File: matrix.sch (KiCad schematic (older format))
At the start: 166 parts

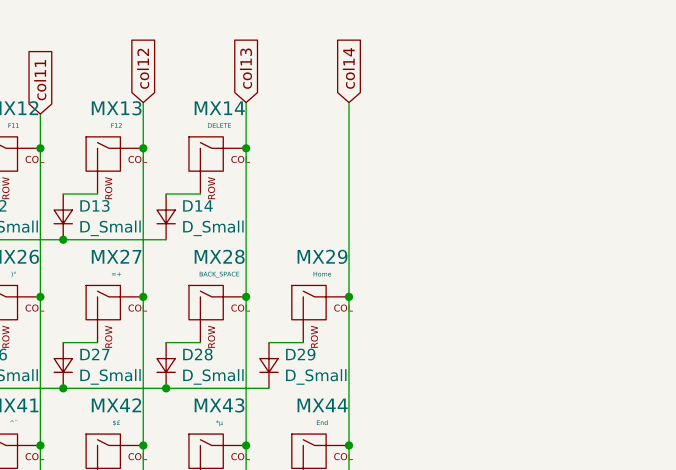
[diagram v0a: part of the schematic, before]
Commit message: Added: rotary encoder to schematics
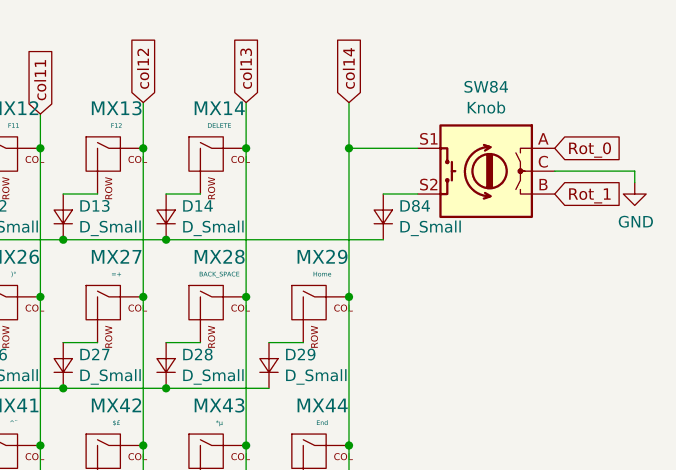
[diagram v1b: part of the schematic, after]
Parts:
- added D84: D_Small, symbol Device:D_Small
- added SW84: Knob, symbol Device:Rotary_Encoder_Switch
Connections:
- net col14: now also SW84.S1
- net row0: now also D84.1 (K)
- new net: D84.2 (A), SW84.S2
- new net GND: SW84.C
- new net Rot_0: SW84.A
- new net Rot_1: SW84.B
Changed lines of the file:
@@
 	6150 3500 7050 3500
-Wire Wire Line
-	7850 900  7850 1750
 Wire Wire Line
 	1550 3100 1550 3750
@@
 Wire Wire Line
 	6950 2400 6950 3750
+Wire Wire Line
+	7850 900  7850 1100
+$Comp
+L Device:Rotary_Encoder_Switch SW84
+U 1 1 66DAE7E9
+P 8450 1200
+F 0 "SW84" H 8450 1567 50  0000 C CNN
+F 1 "Knob" H 8450 1476 50  0000 C CNN
+F 2 "" H 8300 1360 50  0001 C CNN
+F 3 "~" H 8450 1460 50  0001 C CNN
+	1    8450 1200
+	-1   0    0    -1
+$EndComp
+Text GLabel 8750 1100 2    50   Input ~ 0
+Rot_0
+Text GLabel 8750 1300 2    50   Input ~ 0
+Rot_1
+Wire Wire Line
+	8750 1200 9100 1200
+Wire Wire Line
+	9100 1200 9100 1250
+$Comp
+L power:GND #PWR?
+U 1 1 66DD54F4
+P 9100 1250
+F 0 "#PWR?" H 9100 1000 50  0001 C CNN
+F 1 "GND" H 9105 1077 50  0000 C CNN
+F 2 "" H 9100 1250 50  0001 C CNN
+F 3 "" H 9100 1250 50  0001 C CNN
+	1    9100 1250
+	1    0    0    -1
+$EndComp
+Wire Wire Line
+	7850 1100 8150 1100
+$Comp
+L Device:D_Small D84
+U 1 1 66DEA2AC
+P 8000 1400
+F 0 "D84" V 8046 1332 50  0000 R CNN
+F 1 "D_Small" V 7955 1332 50  0000 R CNN
+F 2 "" V 8000 1400 50  0001 C CNN
+F 3 "~" V 8000 1400 50  0001 C CNN
+	1    8000 1400
+	0    -1   -1   0
+$EndComp
+Wire Wire Line
+	7050 1500 8000 1500
+Connection ~ 7050 1500
+Connection ~ 7850 1100
+Wire Wire Line
+	7850 1100 7850 1750
+Wire Wire Line
+	8000 1300 8150 1300
 $EndSCHEMATC
